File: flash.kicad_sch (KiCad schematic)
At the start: 13 parts, among them U1 LFE5U-85F-6BG381C, U10 IS25LP128F-JBLE

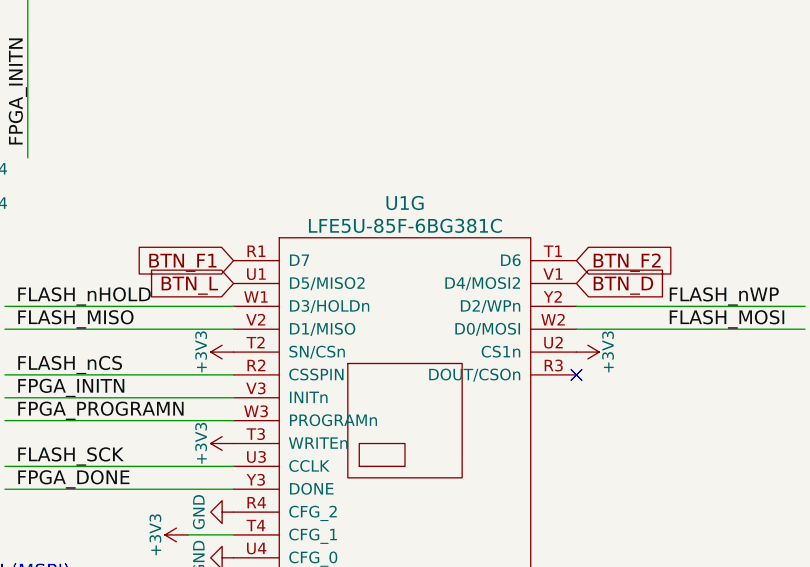
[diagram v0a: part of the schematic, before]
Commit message: remove unneeded components from schema
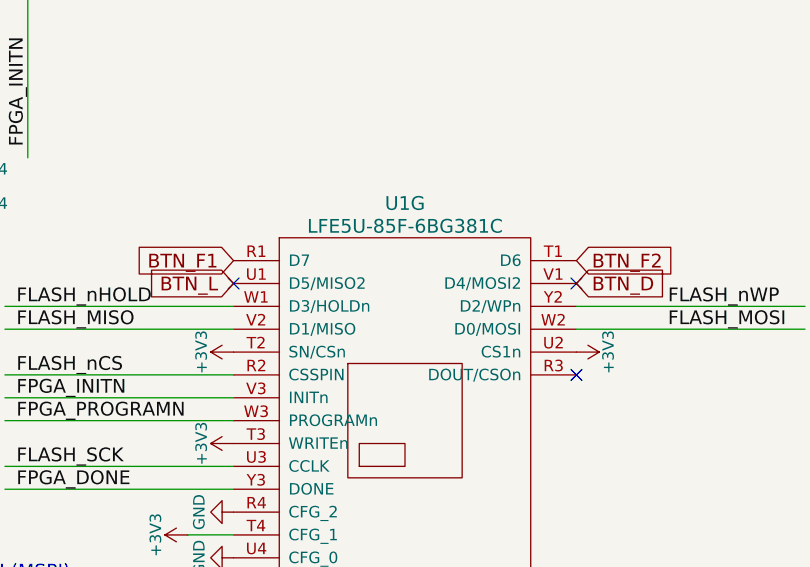
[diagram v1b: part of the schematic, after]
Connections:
- no-connect marks 1 -> 3
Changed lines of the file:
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@@
 		(at 203.2 109.22)
+	)
+	(no_connect
+		(at 165.1 99.06)
+	)
+	(no_connect
+		(at 203.2 99.06)
 	)
 	(wire

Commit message: start to normalize bom
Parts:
- D28, D29: Chip1stop (none) -> C1S541901230010; Digikey (none) -> 1N914BWSCT-ND; LCSC (none) -> C258181; MPN (none) -> 1N4148WS
- R12, R27, R28: Digikey (none) -> 311-10KLMCT-ND; LCSC (none) -> C15401; MPN (none) -> RC0603FR-0710KL
- R30: Digikey (none) -> YAG3613CT-ND; LCSC (none) -> C218056
- R31, R32, R33: Digikey (none) -> YAG3569CT-ND; LCSC (none) -> C217750; MPN (none) -> RC0603FR-0715KL
- U1: Digikey (none) -> 220-2177-ND; LCSC (none) -> C446029

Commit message: updating part numbers across schematcs
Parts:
- D28, D29: MPN 1N4148WS -> 1N4148WS
- R29: Digikey (none) -> 13-AC0603FR-071K1LCT-ND; MPN (none) -> 13-AC0603FR-071K1LCT-ND
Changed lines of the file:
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@@
+			)
+		)
+		(property "Digikey" "13-AC0603FR-071K1LCT-ND"
+			(at 97.79 59.69 90)
+			(effects
+				(font
+					(size 1.27 1.27)
+				)
+				(hide yes)
+			)
+		)
+		(property "MPN" "13-AC0603FR-071K1LCT-ND"
+			(at 97.79 59.69 90)
+			(effects
+				(font
+					(size 1.27 1.27)
+				)
+				(hide yes)
 			)
 		)
@@
 			)
 		)
-		(property "MPN" "1N4148WS "
+		(property "MPN" "1N4148WS"
 			(at 127 90.17 0)
 			(effects
@@
 			)
 		)
-		(property "MPN" "1N4148WS "
+		(property "MPN" "1N4148WS"
 			(at 127 86.36 0)
 			(effects

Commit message: update mouser PN for 4.8kresistor
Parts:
- R30: MPN AC0603FR-104K7L -> 603-RC0603FR-074K7L
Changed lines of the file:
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@@
 			)
 		)
-		(property "MPN" "AC0603FR-104K7L"
+		(property "MPN" "603-RC0603FR-074K7L"
 			(at 102.87 59.69 90)
 			(effects

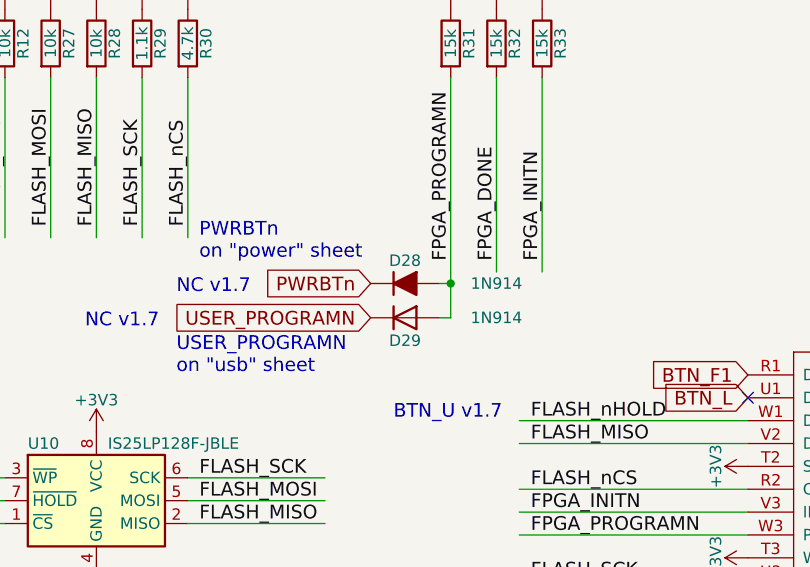
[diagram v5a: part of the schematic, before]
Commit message: Remove 'Leave Empty' in favor of using attributes
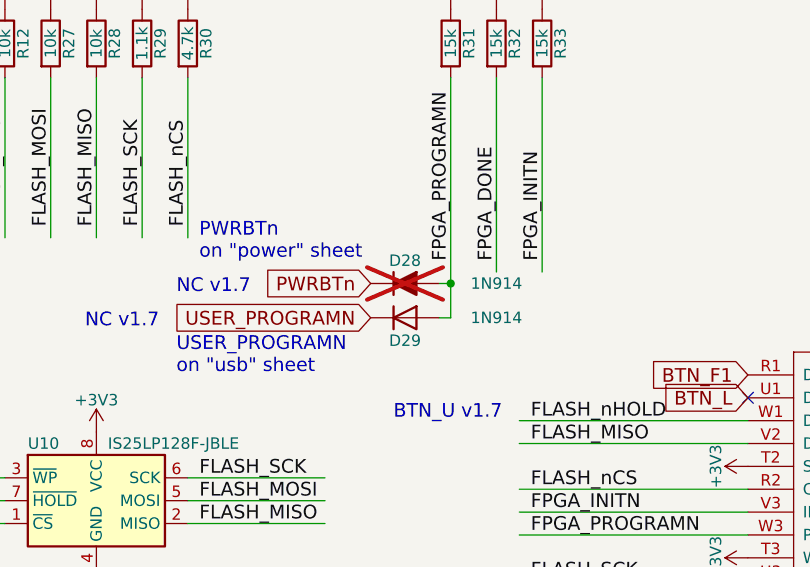
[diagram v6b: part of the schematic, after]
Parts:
- D28: Note Leave empty -> (none); now not fitted
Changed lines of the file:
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@@
 		(in_bom yes)
 		(on_board yes)
-		(in_pos_files yes)
-		(dnp no)
+		(in_pos_files no)
+		(dnp yes)
 		(property "Reference" "D28"
 			(at 127 83.82 0)
@@
 			)
 		)
-		(property "Note" "Leave empty"
+		(property "Note" ""
 			(at 127 86.36 0)
 			(hide yes)

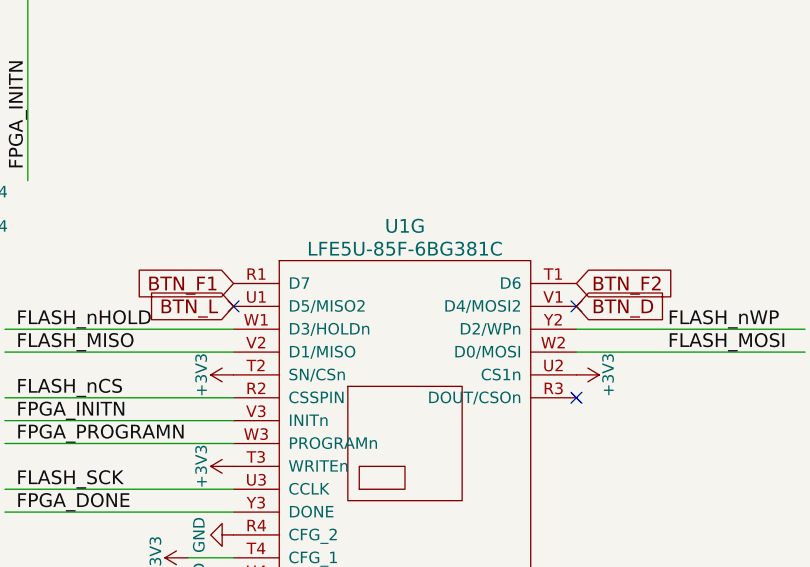
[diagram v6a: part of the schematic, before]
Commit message: remove buttons f1/f2
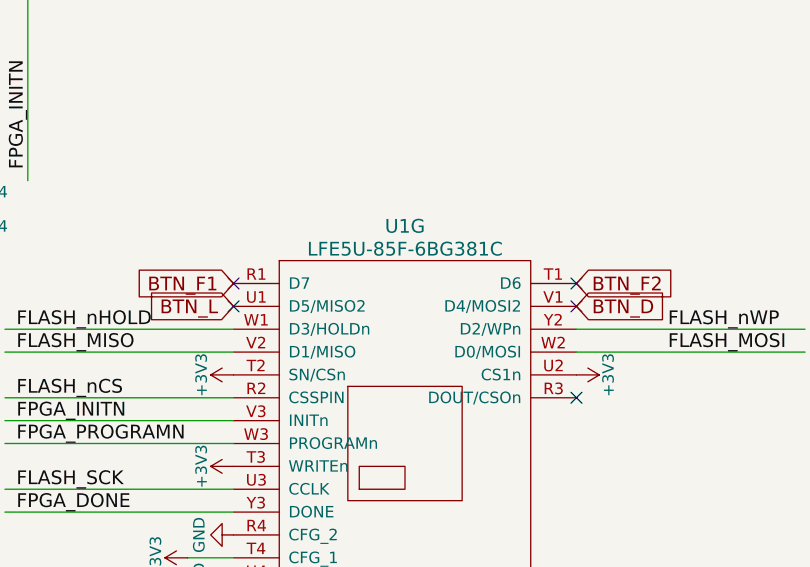
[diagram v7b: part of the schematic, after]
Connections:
- no-connect marks 3 -> 5
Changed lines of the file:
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@@
+	)
+	(no_connect
+		(at 203.2 96.52)
+	)
+	(no_connect
+		(at 165.1 96.52)
 	)
 	(no_connect

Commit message: update parts for 22uf/1uf. Update footprint for RP* items
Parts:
- D28, D29: Digikey 1N914BWSCT-ND -> 1N9148WSCT-ND
